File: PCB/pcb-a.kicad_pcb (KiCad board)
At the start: 2 copper layers, 116.3 x 50.4 mm, 38 parts, among them Q1 BC337, Q2 BC337, Q3 BC337, Q4 BC337, SW1 SW_DIP_x02, U1 MCP23008-xP, U4 ATmega16L-8P

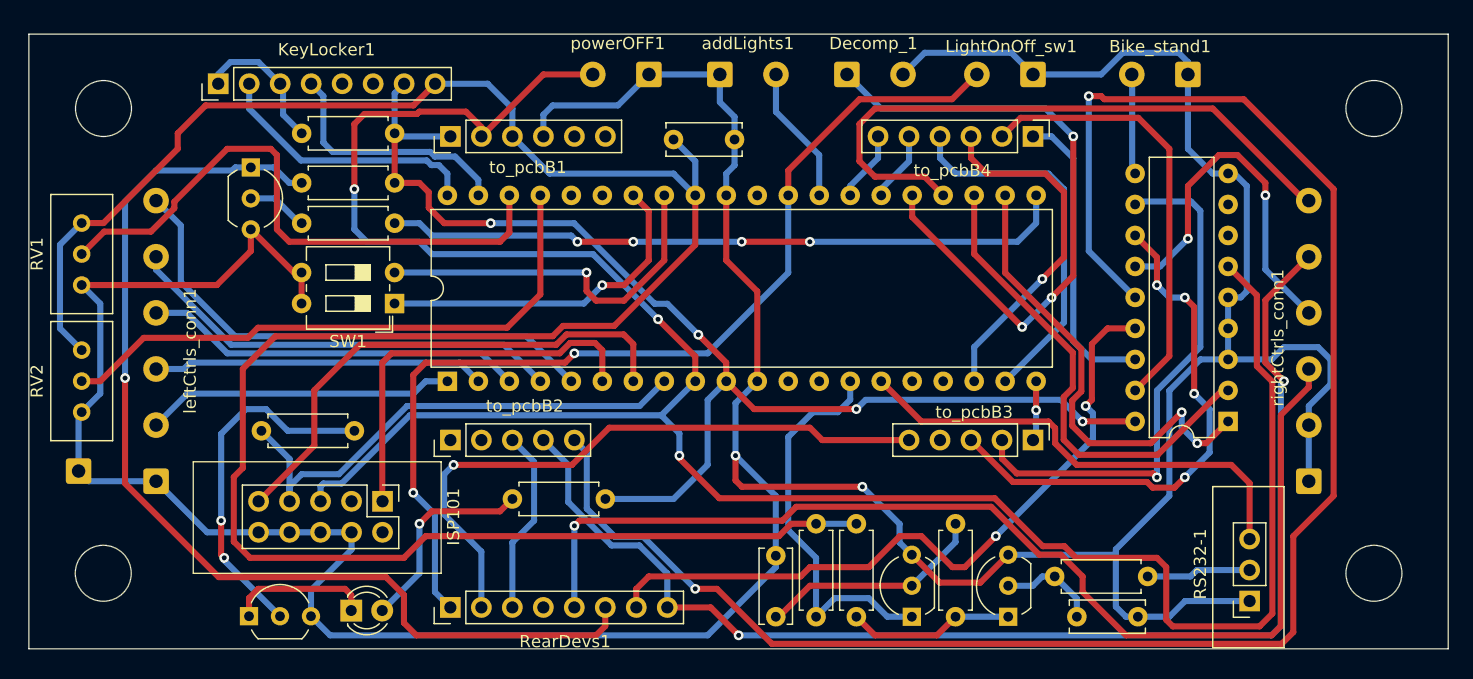
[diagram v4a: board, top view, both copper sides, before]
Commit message: Refactoring: only not critical I/O on MCP23008XP
I know also MCP23008XP is under military standards, but I want my motorbike still be usable after the MCP23008XP is broken
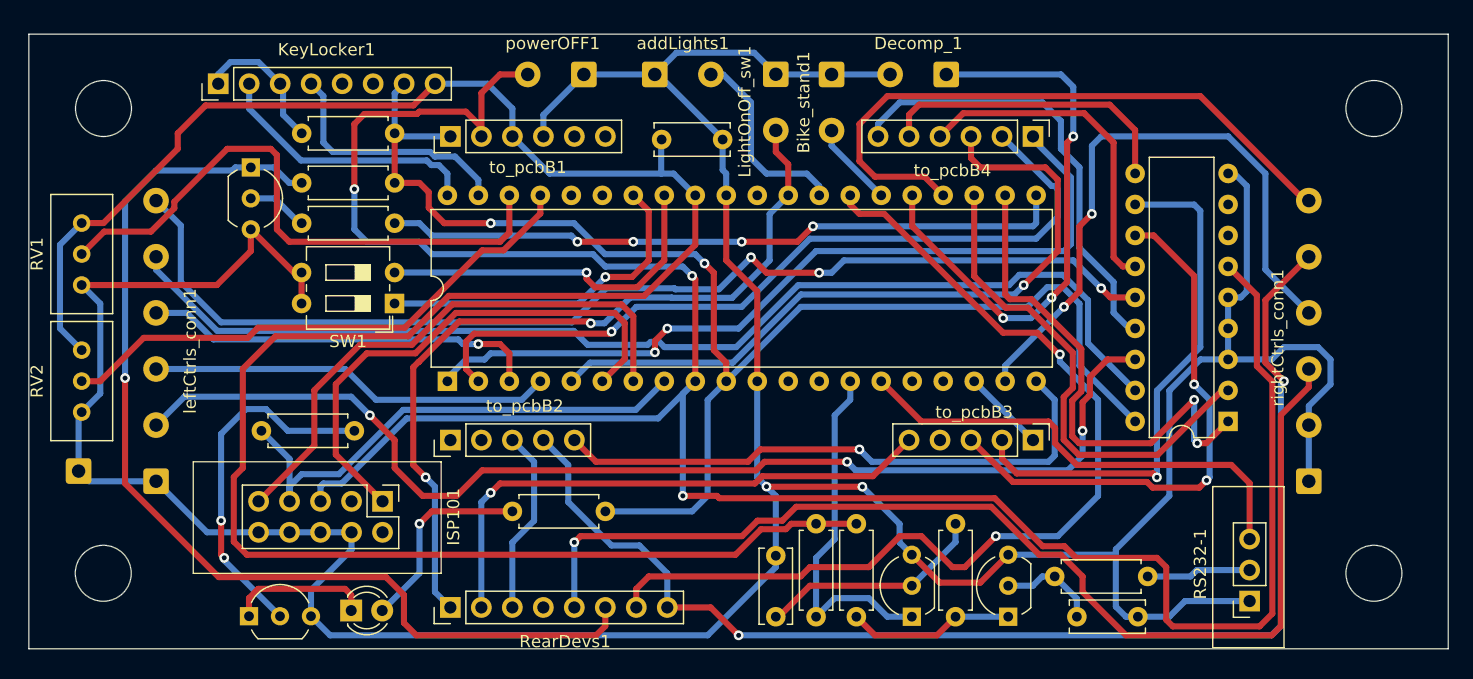
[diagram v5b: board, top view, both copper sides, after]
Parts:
- SW1: value SW_DIP_x02 -> config
- moved Bike_stand1 29.2 mm to (165.4, 59.3), turned to -90 degrees
- moved LightOnOff_sw1 21.1 mm to (160.8, 59.3), turned to -90 degrees
- moved Decomp_1 8.14 mm to (174.8, 59.3), turned to 180 degrees
- moved addLights1 5.33 mm to (150.9, 59.3)
- moved powerOFF1 5.33 mm to (145.1, 59.3)
- moved R9 1.02 mm to (139.2, 95.1)
- moved C2 0.98 mm to (151.4, 64.7)
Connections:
- net Net-(R7-Pad2) renamed o_startEngine
- U1 pad 10: i_bykeStand -> o_rightArrow
- U1 pad 13: i_startButton -> o_horn
- U1 pad 14: o_engineON -> i_horn
- U1 pad 15: i_neutral -> o_leftArrow
- U1 pad 16: o_downLight -> i_leftArrow
- U1 pad 17: o_upLight -> i_rightArrow
- U4 pad 1: i_leftArrow -> o_downLight
- U4 pad 18: o_addLight -> o_keepAlive
- U4 pad 19: o_horn -> i_startButton
- U4 pad 2: i_downLight -> o_upLight
- U4 pad 20: o_keepAlive -> o_engineON
- U4 pad 26: o_rightArrow -> i_bykeStand
- U4 pad 27: o_leftArrow -> i_neutral
- U4 pad 4: i_rightArrow -> i_downLight
- U4 pad 5: i_horn -> o_addLight
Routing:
- net o_engineON: track 147.9 -> 47.9 mm, vias 2 -> 1
- net i_leftArrow: track 25.4 -> 94.6 mm, vias 0 -> 3
- net i_rightArrow: track 36.3 -> 92.6 mm
- net i_horn: track 42.9 -> 91.6 mm, vias 0 -> 3
- net o_downLight: track 24.7 -> 66.6 mm, vias 0 -> 2
- net o_leftArrow: track 5.78 -> 37.2 mm
- net o_addLight: track 29.1 -> 59.8 mm
- net o_upLight: track 36.4 -> 65.1 mm, vias 0 -> 1
- net GND: track 327.6 -> 301.5 mm
- net i_neutral: track 58.5 -> 80.6 mm
- net i_startButton: track 30.1 -> 50.9 mm
- net o_rightArrow: track 5.78 -> 25.4 mm
- net c_rearLight: track 81.6 -> 65.6 mm
- net tempPower: track 101.2 -> 115.6 mm, vias 4 -> 2
- net Net-(ISP101-Pad1): track 32.9 -> 43.2 mm
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
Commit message: small errors and warnings fixed. Ready to be printed
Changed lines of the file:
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@@
   (segment (start 177.051 75.86505) (end 179.633262 78.447312) (width 0.5) (layer "F.Cu") (net 16))
   (segment (start 185.62 90.504) (end 192.094 90.504) (width 0.5) (layer "F.Cu") (net 16))
+  (segment (start 145.276 75.579582) (end 146.467918 76.7715) (width 0.5) (layer "F.Cu") (net 17))
+  (segment (start 149.4385 76.7715) (end 151.651 74.559) (width 0.5) (layer "F.Cu") (net 17))
+  (segment (start 145.276 75.56) (end 145.276 75.579582) (width 0.5) (layer "F.Cu") (net 17))
+  (segment (start 146.467918 76.7715) (end 149.4385 76.7715) (width 0.5) (layer "F.Cu") (net 17))
   (segment (start 151.651 74.559) (end 151.651 69.235) (width 0.5) (layer "F.Cu") (net 17))
-  (segment (start 145.276 76.068) (end 145.9795 76.7715) (width 0.5) (layer "F.Cu") (net 17))
-  (segment (start 145.276 75.56) (end 145.276 76.068) (width 0.5) (layer "F.Cu") (net 17))
-  (segment (start 145.9795 76.7715) (end 149.4385 76.7715) (width 0.5) (layer "F.Cu") (net 17))
-  (segment (start 149.4385 76.7715) (end 151.651 74.559) (width 0.5) (layer "F.Cu") (net 17))
   (via (at 145.276 75.56) (size 0.8) (drill 0.4) (layers "F.Cu" "B.Cu") (net 17))
-  (segment (start 145.276 75.56) (end 145.296 75.58) (width 0.5) (layer "B.Cu") (net 17))
   (segment (start 129.538 75.56) (end 145.276 75.56) (width 0.5) (layer "B.Cu") (net 17))
   (segment (start 149.0185 75.9215) (end 150.376 74.564) (width 0.5) (layer "F.Cu") (net 18))
@@
   (segment (start 144.6415 78.1) (end 129.538 78.1) (width 0.5) (layer "B.Cu") (net 18))
   (segment (start 181.872 89.296) (end 177.051 84.475) (width 0.5) (layer "B.Cu") (net 19))
-  (segment (start 182.126 89.042) (end 181.872 89.296) (width 0.5) (layer "B.Cu") (net 19))
   (segment (start 140.978 91.074) (end 139.2 89.296) (width 0.5) (layer "B.Cu") (net 20))
   (segment (start 139.1945 97.6835) (end 140.978 95.9) (width 0.5) (layer "B.Cu") (net 20))
@@
   (segment (start 171.712 62.626) (end 171.712 64.404) (width 0.5) (layer "F.Cu") (net 21))
   (segment (start 172.536 61.802) (end 171.712 62.626) (width 0.5) (layer "F.Cu") (net 21))
-  (segment (start 190 67.198) (end 190.244 67.442) (width 0.5) (layer "B.Cu") (net 21))
   (segment (start 180.224 92.728) (end 176.792 89.296) (width 0.5) (layer "F.Cu") (net 23))
   (segment (start 195.08 75.834) (end 191.768 72.522) (width 0.5) (layer "F.Cu") (net 23))
@@
   (segment (start 158.504 91.074) (end 146.058 91.074) (width 0.5) (layer "F.Cu") (net 66))
   (segment (start 167.648 90.058) (end 159.52 90.058) (width 0.5) (layer "F.Cu") (net 66))
-  (segment (start 182.126 84.48) (end 182.131 84.475) (width 0.5) (layer "F.Cu") (net 66))
   (via (at 167.648 90.058) (size 0.8) (drill 0.4) (layers "F.Cu" "B.Cu") (net 66))
   (segment (start 183.65 90.566) (end 183.65 85.994) (width 0.5) (layer "B.Cu") (net 66))

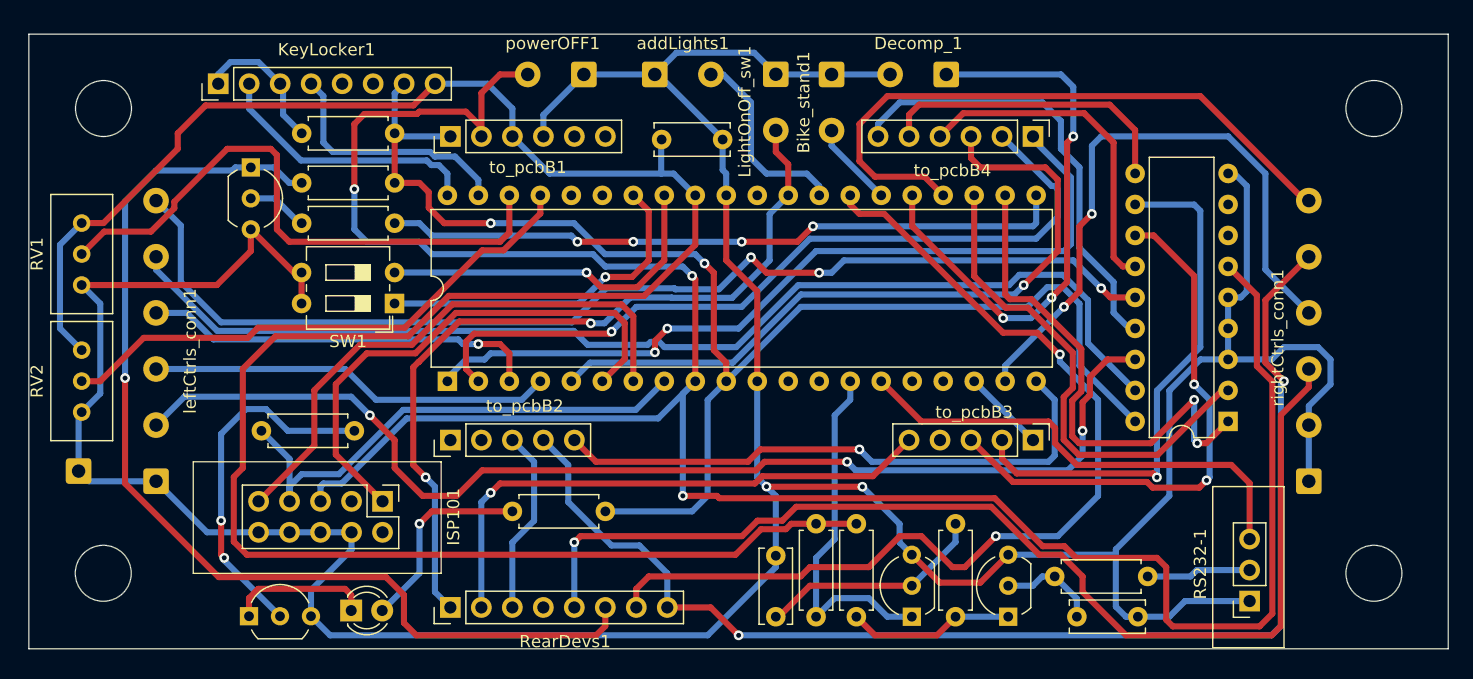
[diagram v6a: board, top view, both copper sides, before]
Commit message: Unusefull components removing and RS232 connected also to PCB-b
- The low-pass filter on RS232 RXD has been removed because external serial cable idea has been dropped
- The RS232 lines are been connected also to the PCB-b for future (CH5 module) Bluetooth implementation
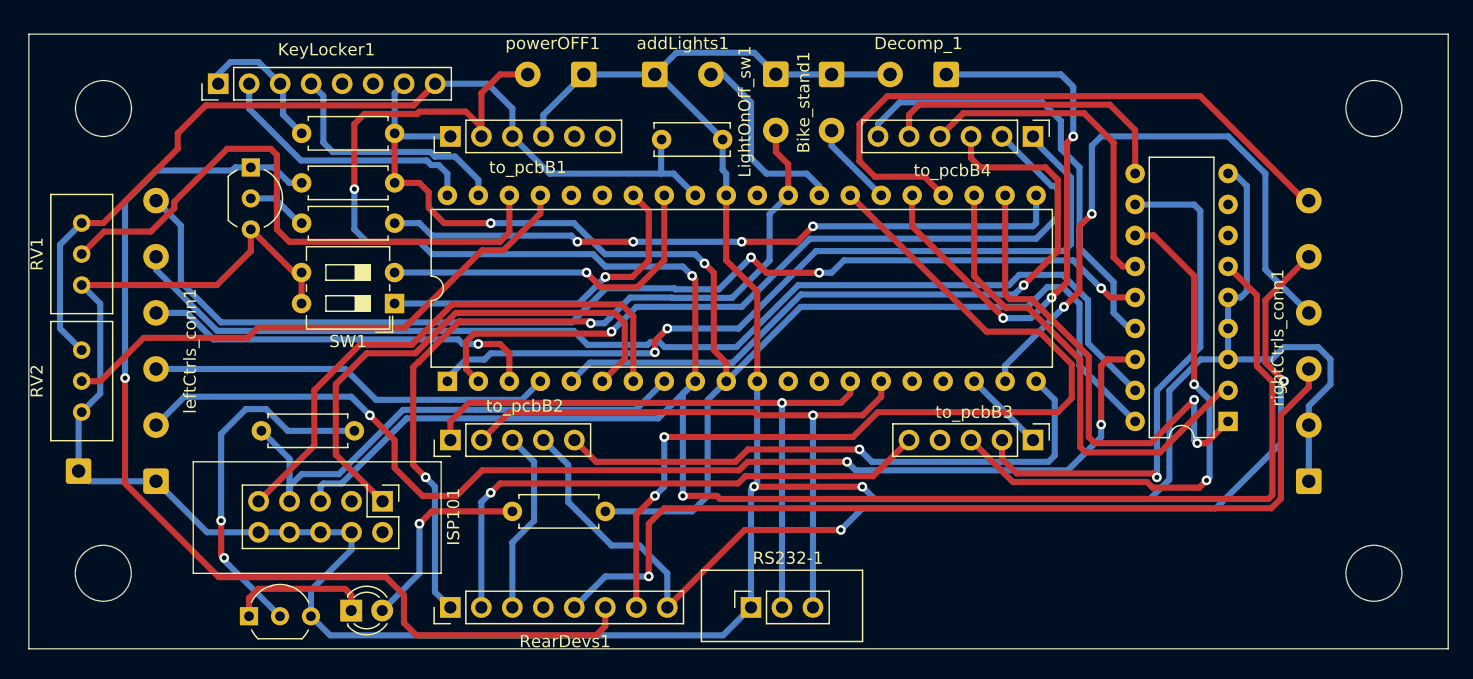
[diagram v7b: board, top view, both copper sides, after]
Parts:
- removed C1, C3: 100nF, Capacitor_THT:C_Disc_D6.0mm_W2.5mm_P5.00mm
- removed Q1, Q2: BC337, Package_TO_SOT_THT:TO-92_Inline_Wide
- removed R2, R3: 10K, Resistor_THT:R_Axial_DIN0207_L6.3mm_D2.5mm_P7.62mm_Horizontal
- removed R4: 2K, Resistor_THT:R_Axial_DIN0207_L6.3mm_D2.5mm_P7.62mm_Horizontal
- removed R5: 100K, Resistor_THT:R_Axial_DIN0207_L6.3mm_D2.5mm_P7.62mm_Horizontal
- moved RS232-1 40.9 mm to (158.8, 103.0), turned to 90 degrees
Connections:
- RS232-1 pad 2: Net-(R2-Pad2) -> c_RS232_RXD
- RS232-1 pad 3: Net-(RS232-1-Pad3) -> c_RS232_TXT
- U4 pad 14: Net-(Q2-Pad1) -> c_RS232_RXD
- U4 pad 15: Net-(RS232-1-Pad3) -> c_RS232_TXT
- to_pcbB2 pad 1: unconnected-(to_pcbB2-Pad1) -> c_RS232_RXD
- to_pcbB2 pad 2: unconnected-(to_pcbB2-Pad2) -> c_RS232_TXT
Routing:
- net +5V: track 188.0 -> 75.6 mm
- net c_RS232_RXD: track 0.00 -> 53.0 mm, vias 0 -> 1
- net c_RS232_TXT: track 0.00 -> 51.5 mm, vias 0 -> 1
- net Net-(RS232-1-Pad3): track 39.0 -> 0.00 mm
- net Net-(Q2-Pad1): track 29.6 -> 0.00 mm
- net GND: track 301.5 -> 278.2 mm
- net Net-(C3-Pad1): track 18.8 -> 0.00 mm
- net i_powerOFF: track 197.8 -> 180.9 mm
- net c_brakeSwitch: track 91.9 -> 75.7 mm
- net Net-(Q1-Pad1): track 13.7 -> 0.00 mm
- net c_engineOFF: track 103.3 -> 92.6 mm
- net Net-(R2-Pad2): track 8.57 -> 0.00 mm
- net Net-(C1-Pad1): track 7.67 -> 0.00 mm
- net i_neutral: track 80.6 -> 76.1 mm
- net Net-(U1-Pad1): track 42.3 -> 40.9 mm
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
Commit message: Less wasted electric power when mb is turned off
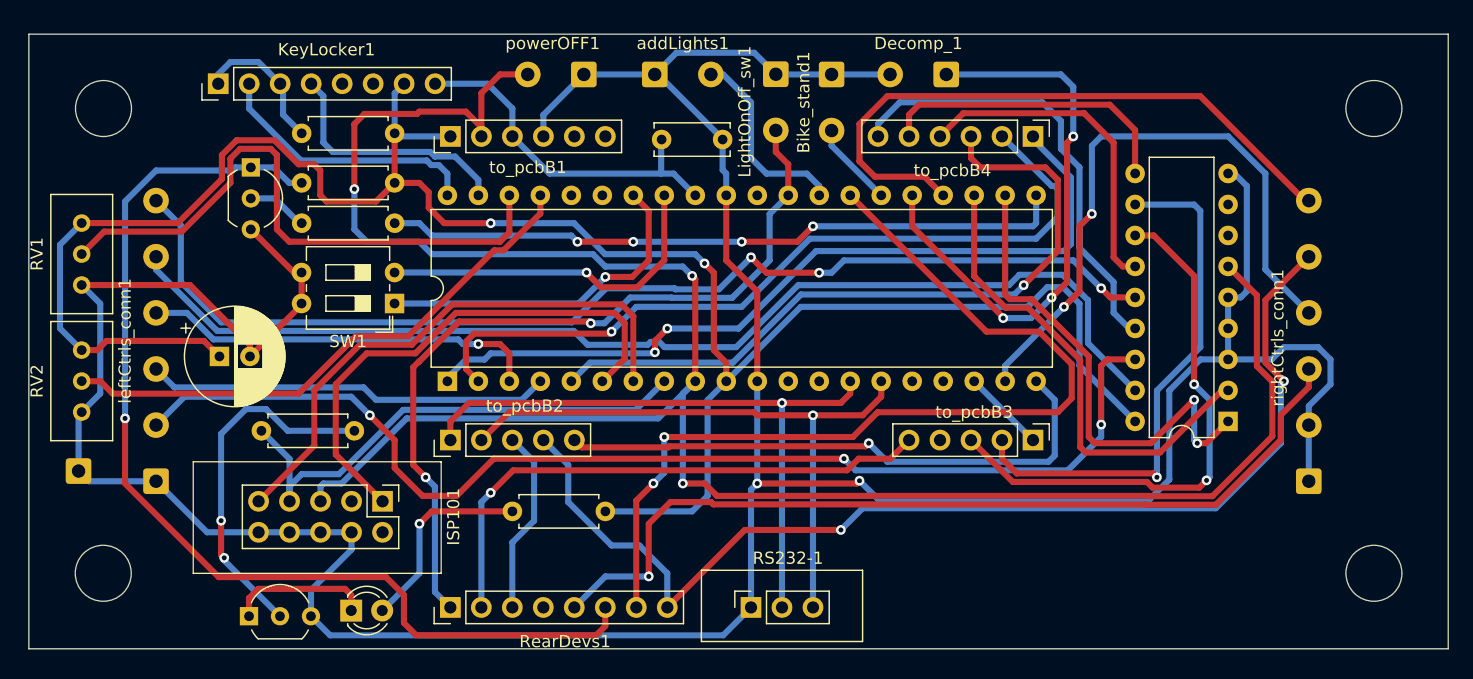
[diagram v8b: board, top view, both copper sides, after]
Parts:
- added C1: 100uf, Capacitor_THT:CP_Radial_D8.0mm_P2.50mm, F.Cu at (115.2, 82.4)
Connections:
- RV1 pad 1: +5V -> tempPower
- RV2 pad 1: +5V -> tempPower
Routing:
- net tempPower: track 115.6 -> 173.1 mm
- net +5V: track 75.6 -> 29.3 mm
- net GND: track 278.2 -> 284.3 mm
- net i_powerOFF: track 180.9 -> 177.3 mm
- net c_brakeSwitch: track 75.7 -> 73.1 mm
- net Net-(RV1-Pad2): track 49.0 -> 49.9 mm
- net Net-(RV2-Pad2): track 44.8 -> 45.6 mm
- net o_engineON: track 47.9 -> 47.3 mm
